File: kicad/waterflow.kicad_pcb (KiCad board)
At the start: 2 copper layers, 38 x 65.8 mm, 15 parts, among them J1 Terminal, Q1 locked, Q2 locked, U1 WeMos_D1_mini

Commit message: fixed: LED+ is now LOUT
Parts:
- removed R3: 510, Resistor_THT:R_Axial_DIN0207_L6.3mm_D2.5mm_P10.16mm_Horizontal
- renumbered 4.7uF to C1, AO4447 to Q3
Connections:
- J1 pad 7: LED+ -> LatchOut
- Q3 pad 5: Net-(R2-Pad1) -> LatchOut
- Q3 pad 6: Net-(R2-Pad1) -> LatchOut
- R2 pad 1: Net-(R2-Pad1) -> LatchOut
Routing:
- net Net-(C1-Pad1): track 91.7 -> 48.3 mm
- net LatchOut: track 0.00 -> 40.1 mm
- net Net-(R2-Pad1): track 19.6 -> 0.00 mm
- net LED+: track 10.3 -> 0.00 mm
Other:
- board text added: "LOUT"
- board text removed: "LED+"

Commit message: added: polarity labels for C1
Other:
- board text added: "+"
- board text added: "-"
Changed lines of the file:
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@@
     (property "Sheetname" "")
     (attr through_hole)
-    (fp_text reference "C1" (at 2.5 0) (layer "F.SilkS")
+    (fp_text reference "C1" (at 1.9 1.61) (layer "F.SilkS") hide
       (effects (font (size 0.7 0.7) (thickness 0.12)))
     )
-    (fp_text value "4.7uF" (at 2.5 2.2) (layer "F.Fab")
-      (effects (font (size 1 1) (thickness 0.15)))
+    (fp_text value "4.7uF" (at 2.5 -0.14) (layer "F.SilkS")
+      (effects (font (size 0.7 0.7) (thickness 0.125)))
     )
     (fp_text user "${REFERENCE}" (at 2.5 0) (layer "F.Fab")
@@
     (effects (font (size 1 1) (thickness 0.15)))
   )
+  (gr_text "+" (at 101.4 37.5) (layer "F.SilkS")
+    (effects (font (size 1 1) (thickness 0.15)))
+  )
   (gr_text "SWITCH" (at 106.25 77.45) (layer "F.SilkS")
     (effects (font (size 1 1) (thickness 0.15)))
@@
     (effects (font (size 1.25 1.25) (thickness 0.15)))
   )
+  (gr_text "-" (at 96.4 37.5) (layer "F.SilkS")
+    (effects (font (size 1 1) (thickness 0.15)))
+  )
   (segment (start 107.65 44.61) (end 107.65 45.86) (width 0.3) (layer "F.Cu") (net 1))

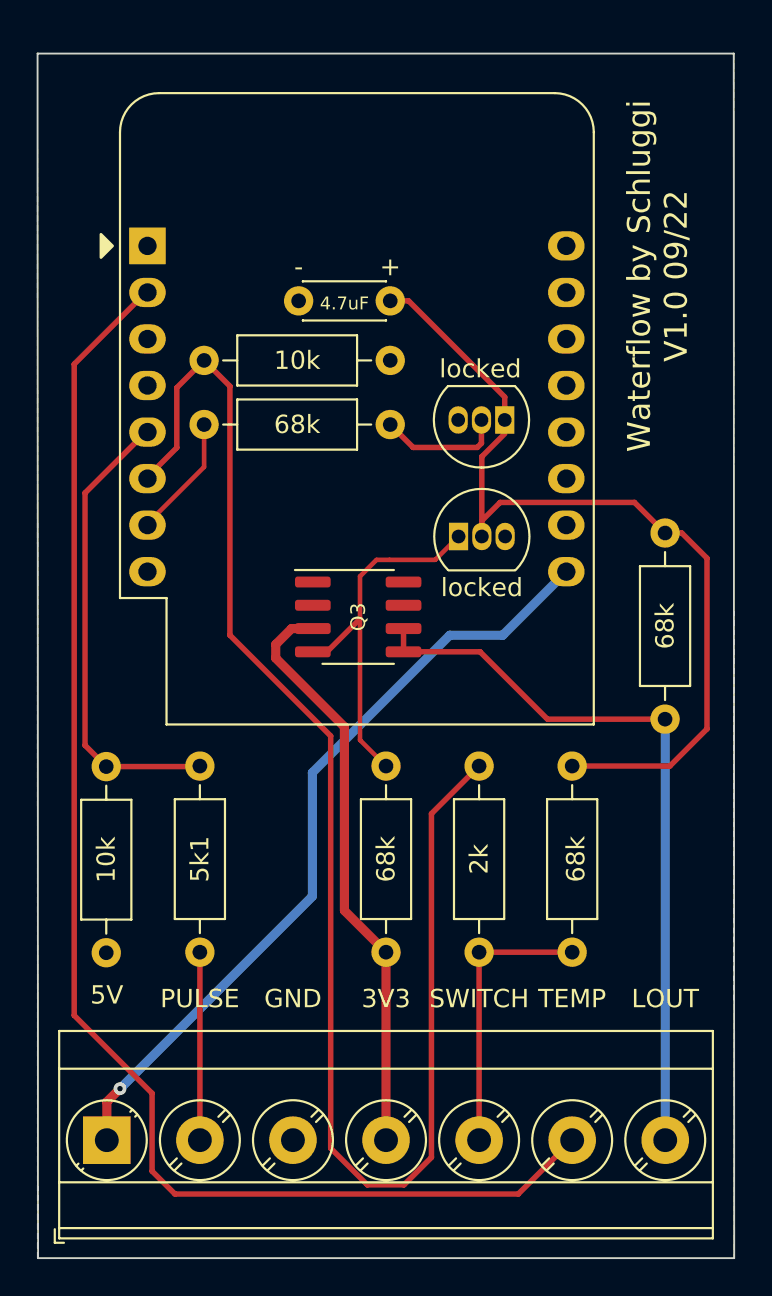
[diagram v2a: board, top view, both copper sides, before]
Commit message: changed: footprint for BC547 (make soldering easier)
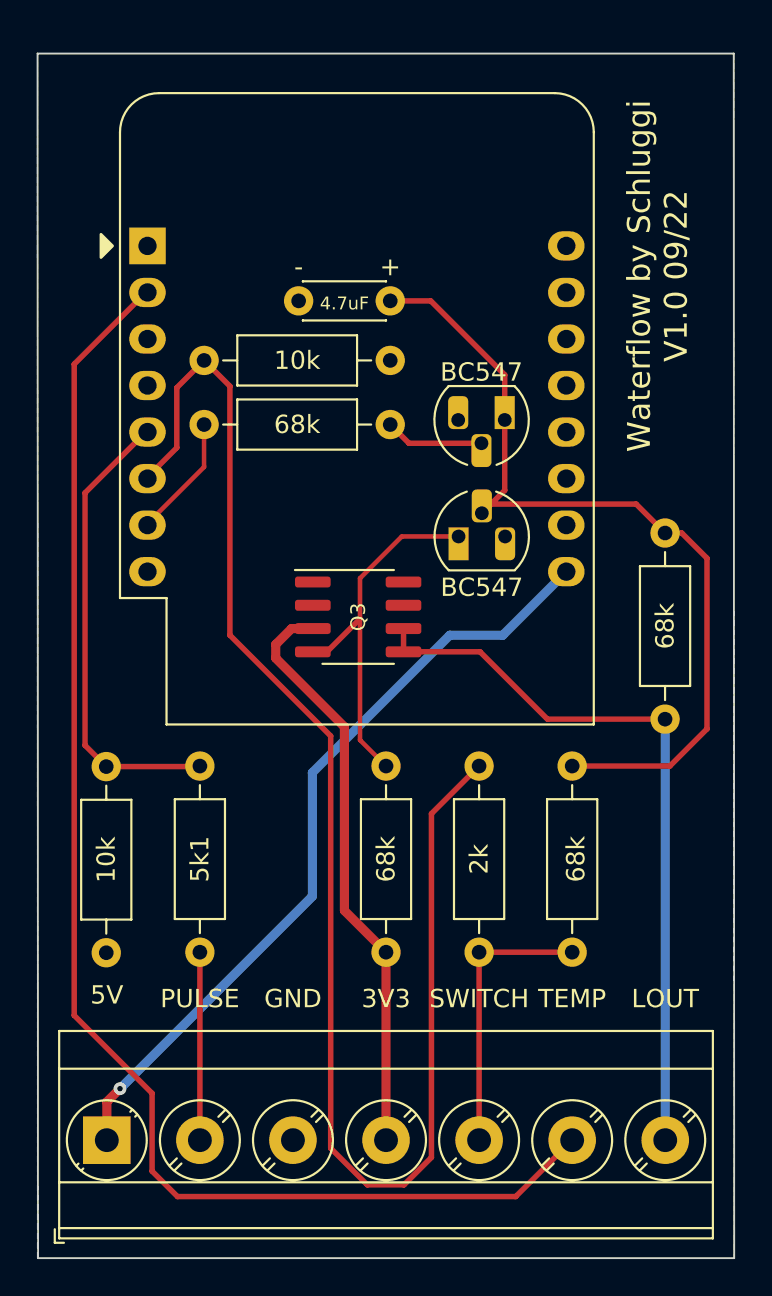
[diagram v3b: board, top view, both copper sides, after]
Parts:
- BC547: renamed from Q2; footprint Package_TO_SOT_THT:TO-92_Inline -> Package_TO_SOT_THT:TO-92_HandSolder
- BC547: renamed from Q1; footprint Package_TO_SOT_THT:TO-92_Inline -> Package_TO_SOT_THT:TO-92_HandSolder
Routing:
- net Net-(Q2-Pad2): track 6.86 -> 5.40 mm
- net Net-(C1-Pad1): track 48.3 -> 47.4 mm

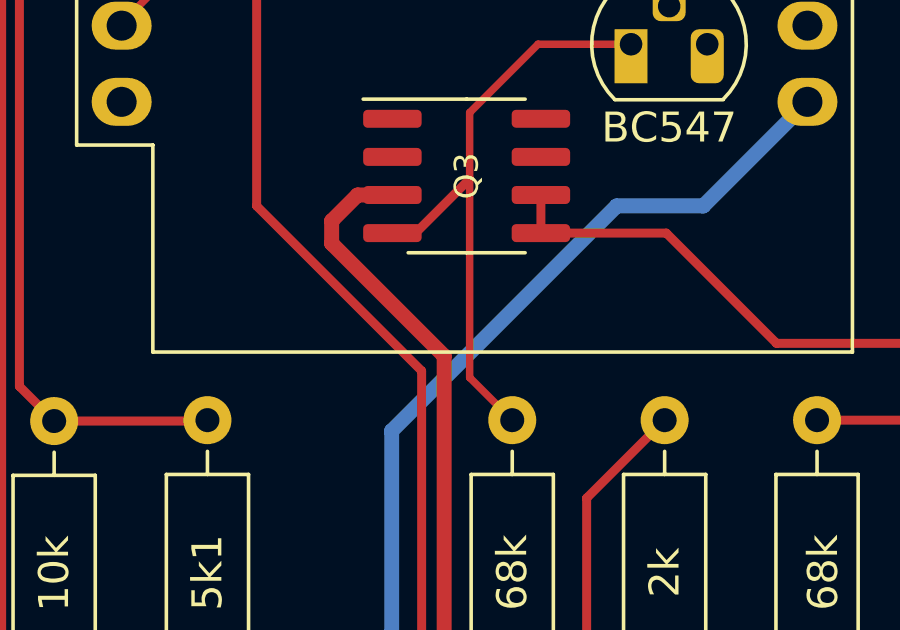
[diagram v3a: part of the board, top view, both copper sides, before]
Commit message: added: usb label for orientation
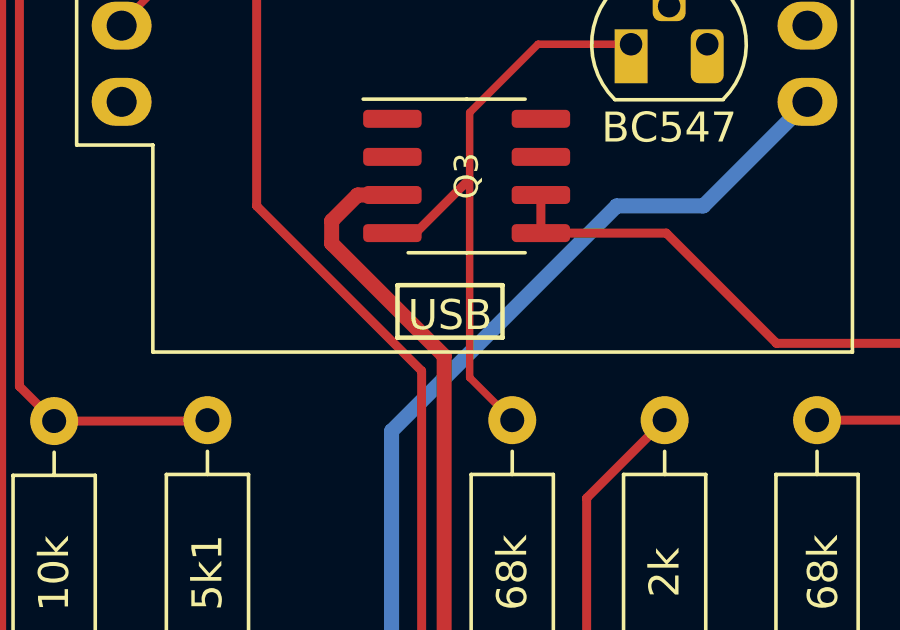
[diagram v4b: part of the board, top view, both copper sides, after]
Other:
- board text added: "USB"
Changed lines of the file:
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@@
     )
   )
+  (gr_line (start 100.845 60.25) (end 100.845 62) (layer "F.SilkS") (width 0.15))
+  (gr_line (start 97.345 60.25) (end 100.845 60.25) (layer "F.SilkS") (width 0.15))
+  (gr_line (start 97.345 62) (end 97.345 60.25) (layer "F.SilkS") (width 0.15))
+  (gr_line (start 100.845 62) (end 97.345 62) (layer "F.SilkS") (width 0.15))
   (gr_line (start 82.15 25.86) (end 82.175 91.61) (layer "Edge.Cuts") (width 0.1))
   (gr_line (start 120.175 91.61) (end 120.15 25.86) (layer "Edge.Cuts") (width 0.1))
   (gr_line locked (start 120.15 25.86) (end 82.15 25.86) (layer "Edge.Cuts") (width 0.1))
   (gr_line (start 120.175 91.61) (end 82.175 91.61) (layer "Edge.Cuts") (width 0.1))
+  (gr_text "USB" (at 99.095 61.25) (layer "F.SilkS")
+    (effects (font (size 1 1) (thickness 0.15)))
+  )
   (gr_text "PULSE" (at 91.01 77.45) (layer "F.SilkS")
     (effects (font (size 1 1) (thickness 0.15)))
@@
     )
   )
+  (group "" (id 7d1ae0e0-3f48-466d-8b6d-d9aa51d7d16b)
+    (members
+      2141c75c-5c14-49bf-942d-3746ab61b706
+      42bbebaa-9bdc-4a74-b31b-ca0120989c48
+      49fa48da-6dbb-4137-8bad-0fd869f11151
+      906fe4e1-427b-4e69-9bf7-f5ab9363faa2
+    )
+  )
+  (group "" (id a03b5ad8-f9fd-4108-9b7b-cb52db29b27a)
+    (members
+      190b516c-eafe-4260-a33e-1efc8512da4c
+      7d1ae0e0-3f48-466d-8b6d-d9aa51d7d16b
+    )
+  )

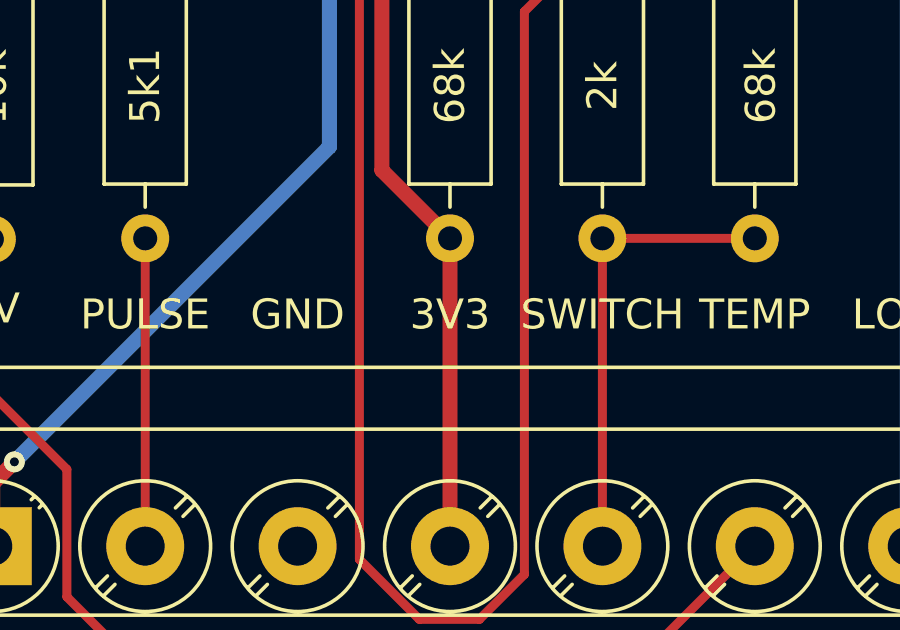
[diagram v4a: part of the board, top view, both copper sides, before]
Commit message: changed: label 3V3 -> VCC
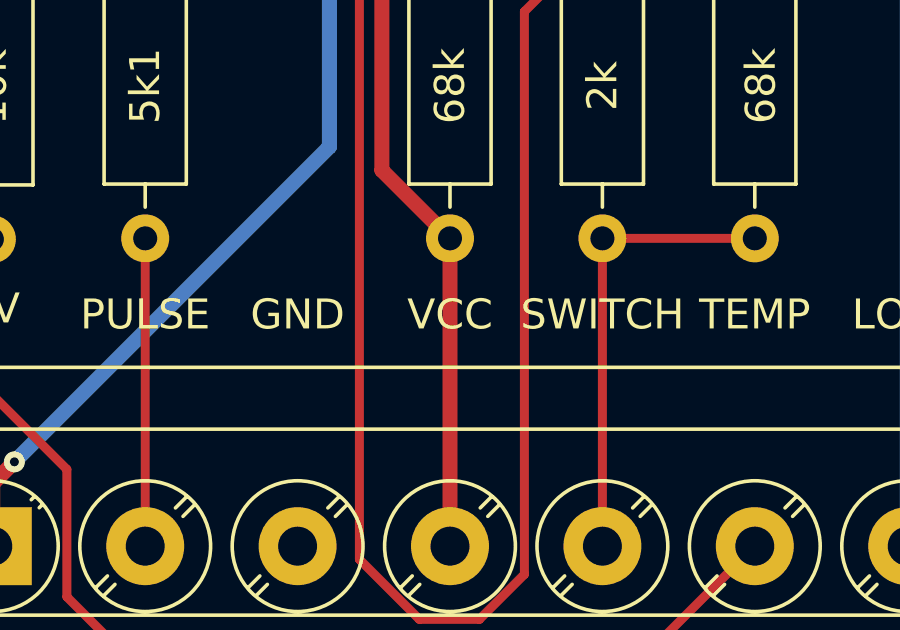
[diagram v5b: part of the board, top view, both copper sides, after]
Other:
- board text added: "VCC"
- board text removed: "3V3"
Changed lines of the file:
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@@
     (effects (font (size 1 1) (thickness 0.15)))
   )
-  (gr_text "3V3\n" (at 101.17 77.45) (layer "F.SilkS")
+  (gr_text "VCC" (at 101.17 77.45) (layer "F.SilkS")
     (effects (font (size 1 1) (thickness 0.15)))
   )

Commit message: release v1.1
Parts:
- added R3: 22K, Resistor_THT:R_Axial_DIN0207_L6.3mm_D2.5mm_P10.16mm_Horizontal, F.Cu at (92.2, 36.4)
- moved R7 19.1 mm to (92.2, 59.3), turned to 90 degrees
- moved R5 12.0 mm to (99.2, 37.2), turned to -90 degrees
- moved C1 6.16 mm to (107.5, 40.2)
- moved R2 1.71 mm to (117.2, 60.7)
- renumbered BC547 to Q1, BC547 to Q2
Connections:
- net 3V3 renamed VCC
- J1 pad 6: Temperature -> LatchOut
- J1 pad 7: LatchOut -> Temperature
- U1 pad 13: unconnected-(U1-Pad13) -> Net-(R5-Pad1)
- U1 pad 3: unconnected-(U1-Pad3) -> Net-(R3-Pad2)
- U1 pad 7: Net-(R5-Pad1) -> unconnected-(U1-Pad7)
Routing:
- net Temperature: track 76.3 -> 90.6 mm
- net Net-(R5-Pad1): track 6.61 -> 16.5 mm
- net Net-(R6-Pad2): track 82.8 -> 73.1 mm
- net Net-(R3-Pad2): track 0.00 -> 7.30 mm
- net Net-(C1-Pad1): track 47.4 -> 42.0 mm
- net LatchOut: track 40.1 -> 44.2 mm
- net Net-(Q2-Pad2): track 5.40 -> 7.21 mm
- net 5V: track 43.2 -> 42.7 mm, vias 1 -> 0
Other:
- board text added: "3V3"
- board text added: "A0"
- board text added: "D0"
- board text added: "D1"
- board text added: "D2"
- board text added: "D3"
- board text added: "D4"
- board text added: "D5"
- board text added: "D6"
- board text added: "D7"
- board text added: "D8"
- board text added: "RST"
- board text added: "RX"
- board text added: "TX"
- board text added: "Waterflow by Schluggi V1.1 10/22"
- board text removed: "Waterflow by Schluggi V1.0 09/22"
